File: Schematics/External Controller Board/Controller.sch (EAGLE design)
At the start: 11 parts, among them U1 TEENSY2, U2 JOYSTICK

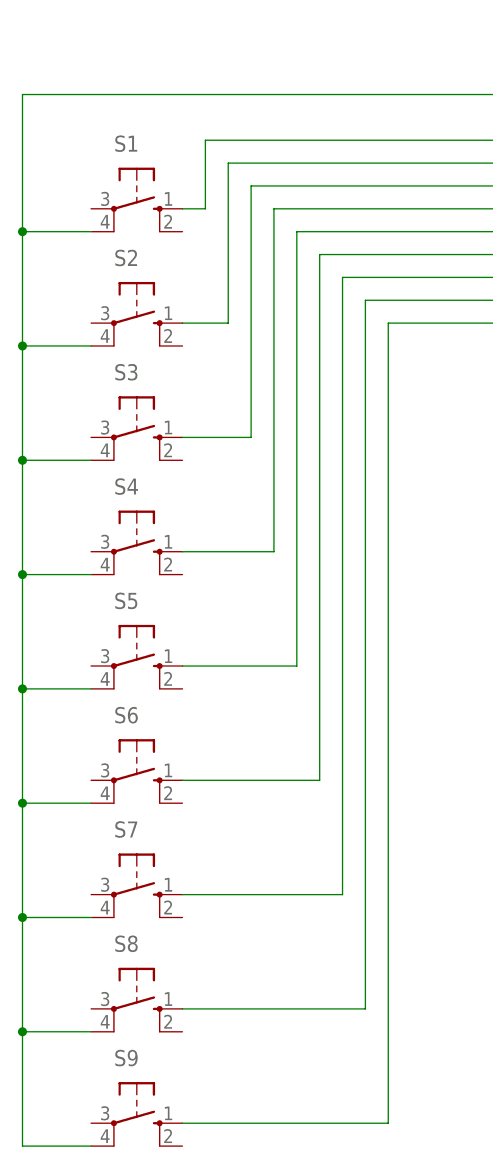
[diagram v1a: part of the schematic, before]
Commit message: Schematics updated External Controller board schematic created
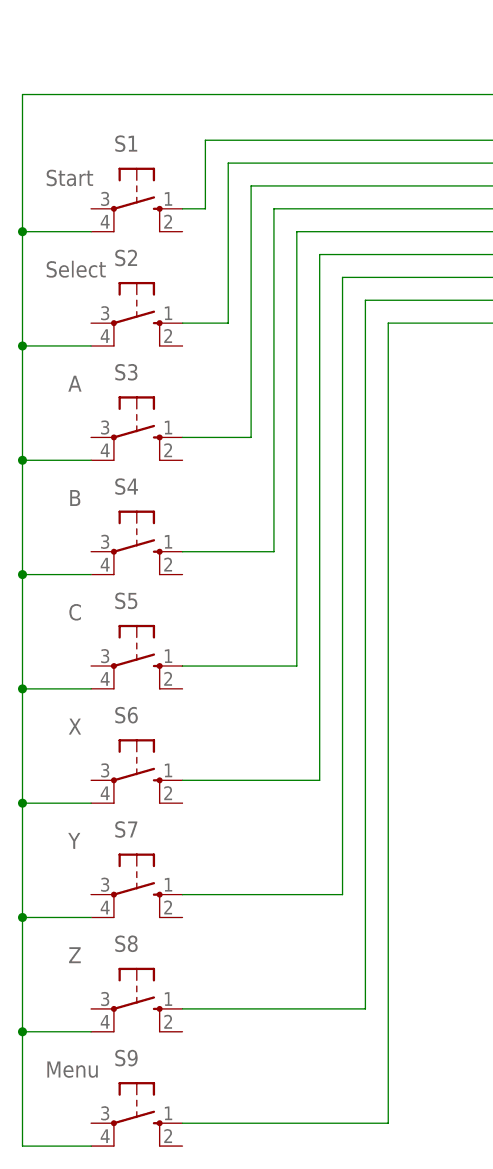
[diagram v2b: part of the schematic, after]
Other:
- note added: "A"
- note added: "B"
- note added: "C"
- note added: "Menu"
- note added: "Select"
- note added: "Start"
- note added: "X"
- note added: "Y"
- note added: "Z"
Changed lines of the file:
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@@
 <setting verticaltext="up"/>
 </settings>
-<grid distance="0.1" unitdist="inch" unit="inch" style="lines" multiple="1" display="no" altdistance="0.01" altunitdist="inch" altunit="inch"/>
+<grid distance="0.1" unitdist="inch" unit="inch" style="lines" multiple="1" display="yes" altdistance="0.01" altunitdist="inch" altunit="inch"/>
 <layers>
 <layer number="1" name="Top" color="4" fill="1" visible="no" active="no"/>
@@
 <sheet>
 <plain>
+<text x="58.42" y="137.16" size="1.778" layer="96">Start</text>
+<text x="58.42" y="127" size="1.778" layer="96">Select</text>
+<text x="58.42" y="38.1" size="1.778" layer="96">Menu</text>
+<text x="60.96" y="114.3" size="1.778" layer="96">A</text>
+<text x="60.96" y="101.6" size="1.778" layer="96">B</text>
+<text x="60.96" y="88.9" size="1.778" layer="96">C</text>
+<text x="60.96" y="76.2" size="1.778" layer="96">X</text>
+<text x="60.96" y="63.5" size="1.778" layer="96">Y</text>
+<text x="60.96" y="50.8" size="1.778" layer="96">Z</text>
 </plain>
 <instances>

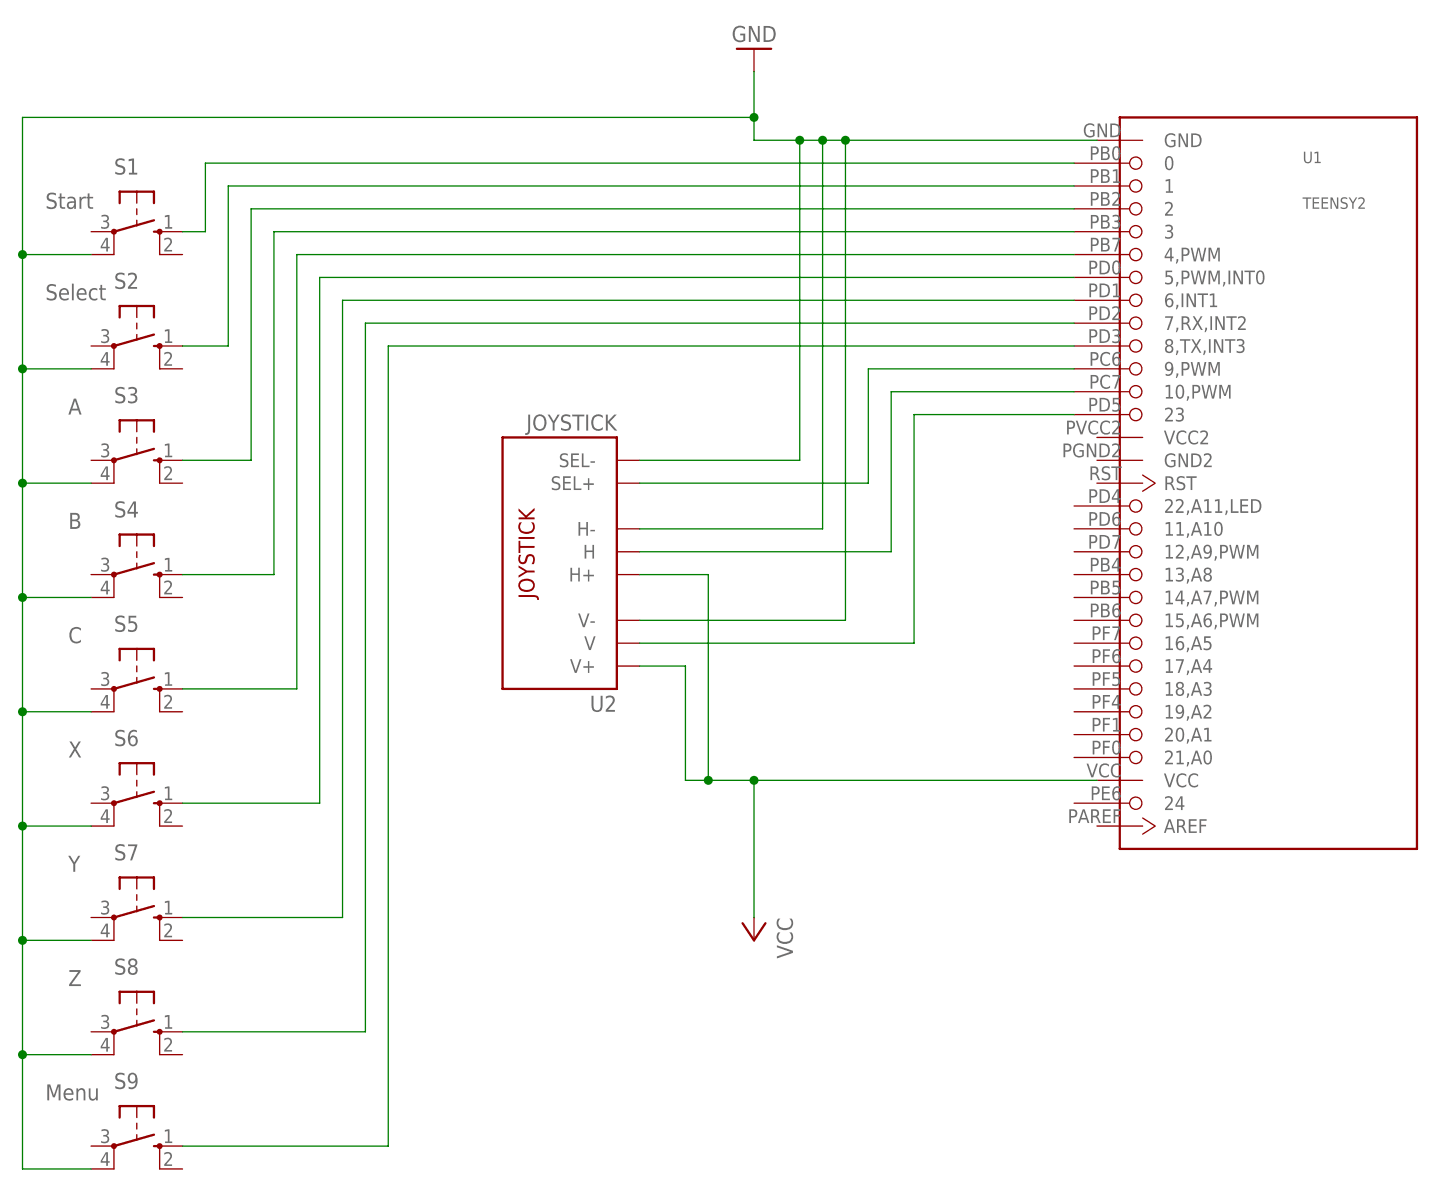
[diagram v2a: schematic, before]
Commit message: Updated the schematics for the external controller.
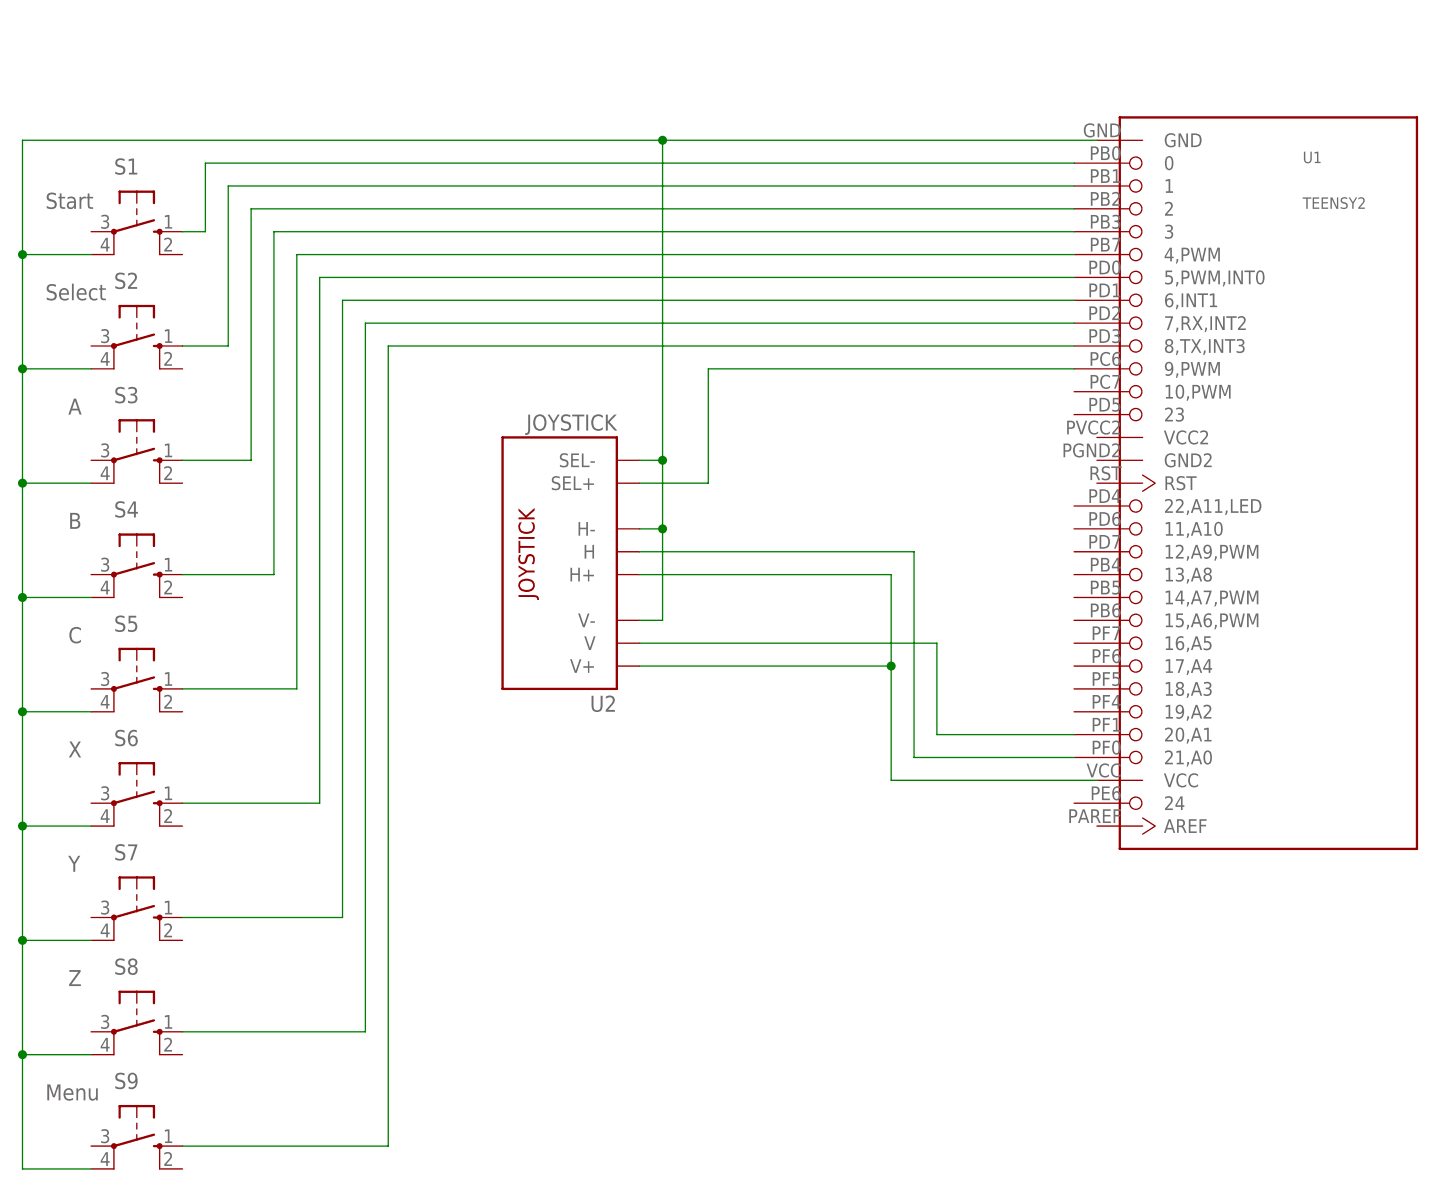
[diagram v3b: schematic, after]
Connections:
- net GND renamed N$13
- net VCC renamed N$10
- removed net N$10 (its old number): U1.10,PWM, U2.H
- removed net N$9 (its old number): U1.23, U2.V
- new net N$11: U1.21,A0, U2.H
- new net N$14: U1.20,A1, U2.V
